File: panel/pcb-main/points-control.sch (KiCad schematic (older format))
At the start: 76 parts

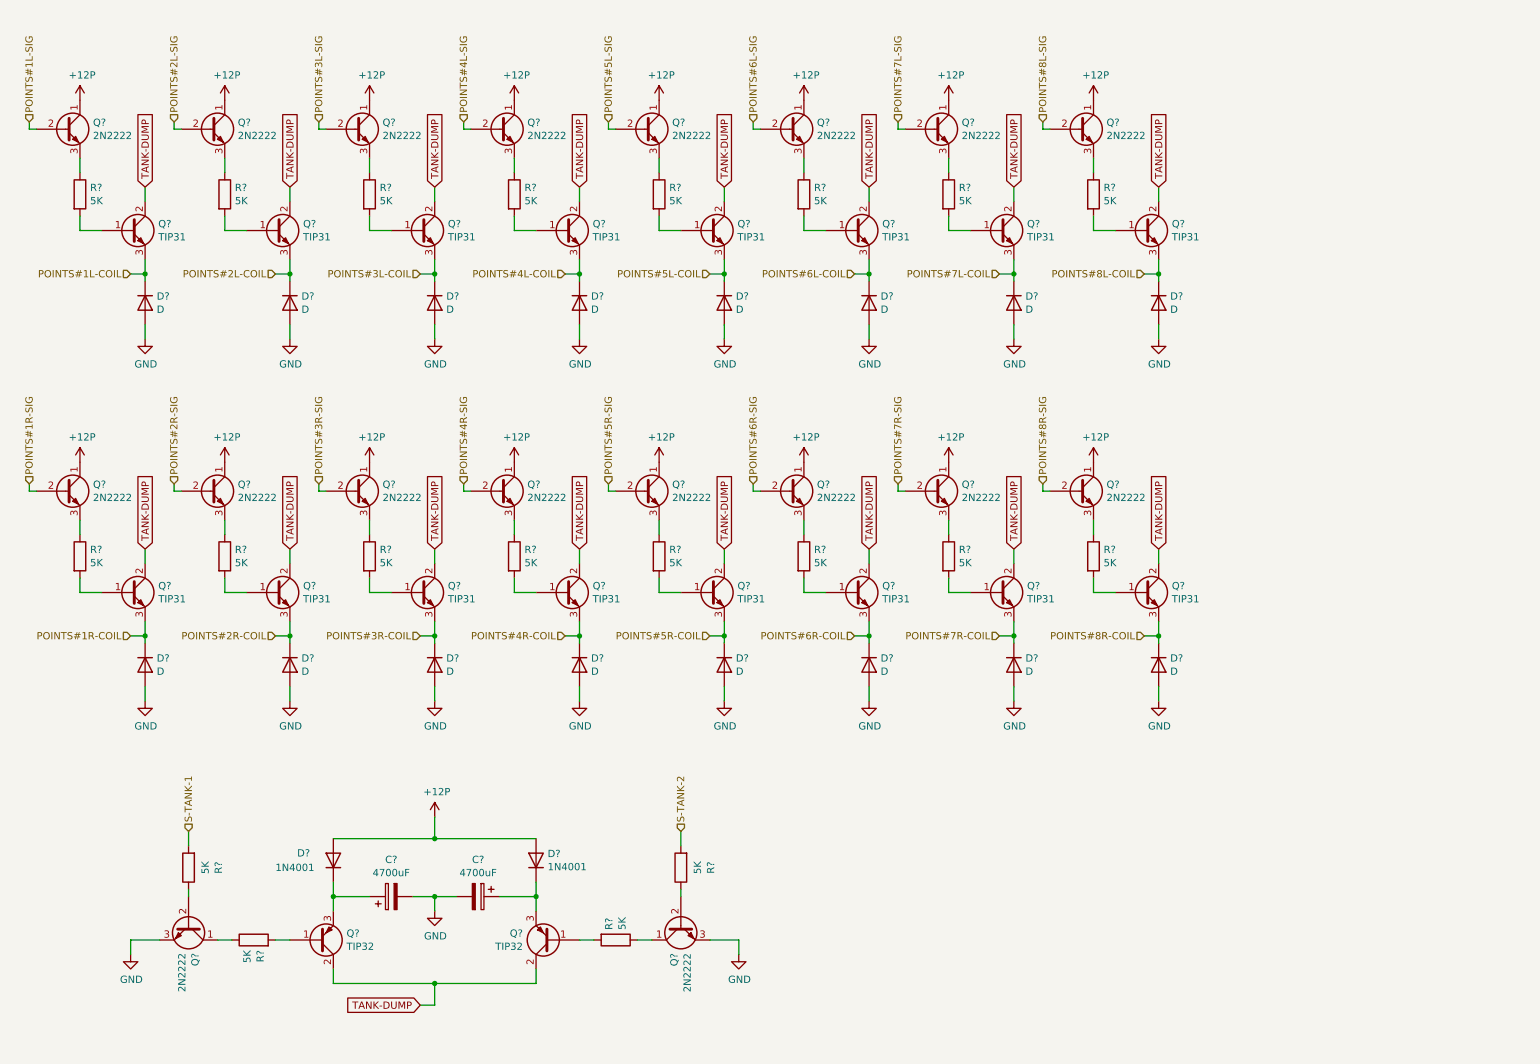
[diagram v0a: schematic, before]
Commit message: PCB Updates and added panel-fw project.
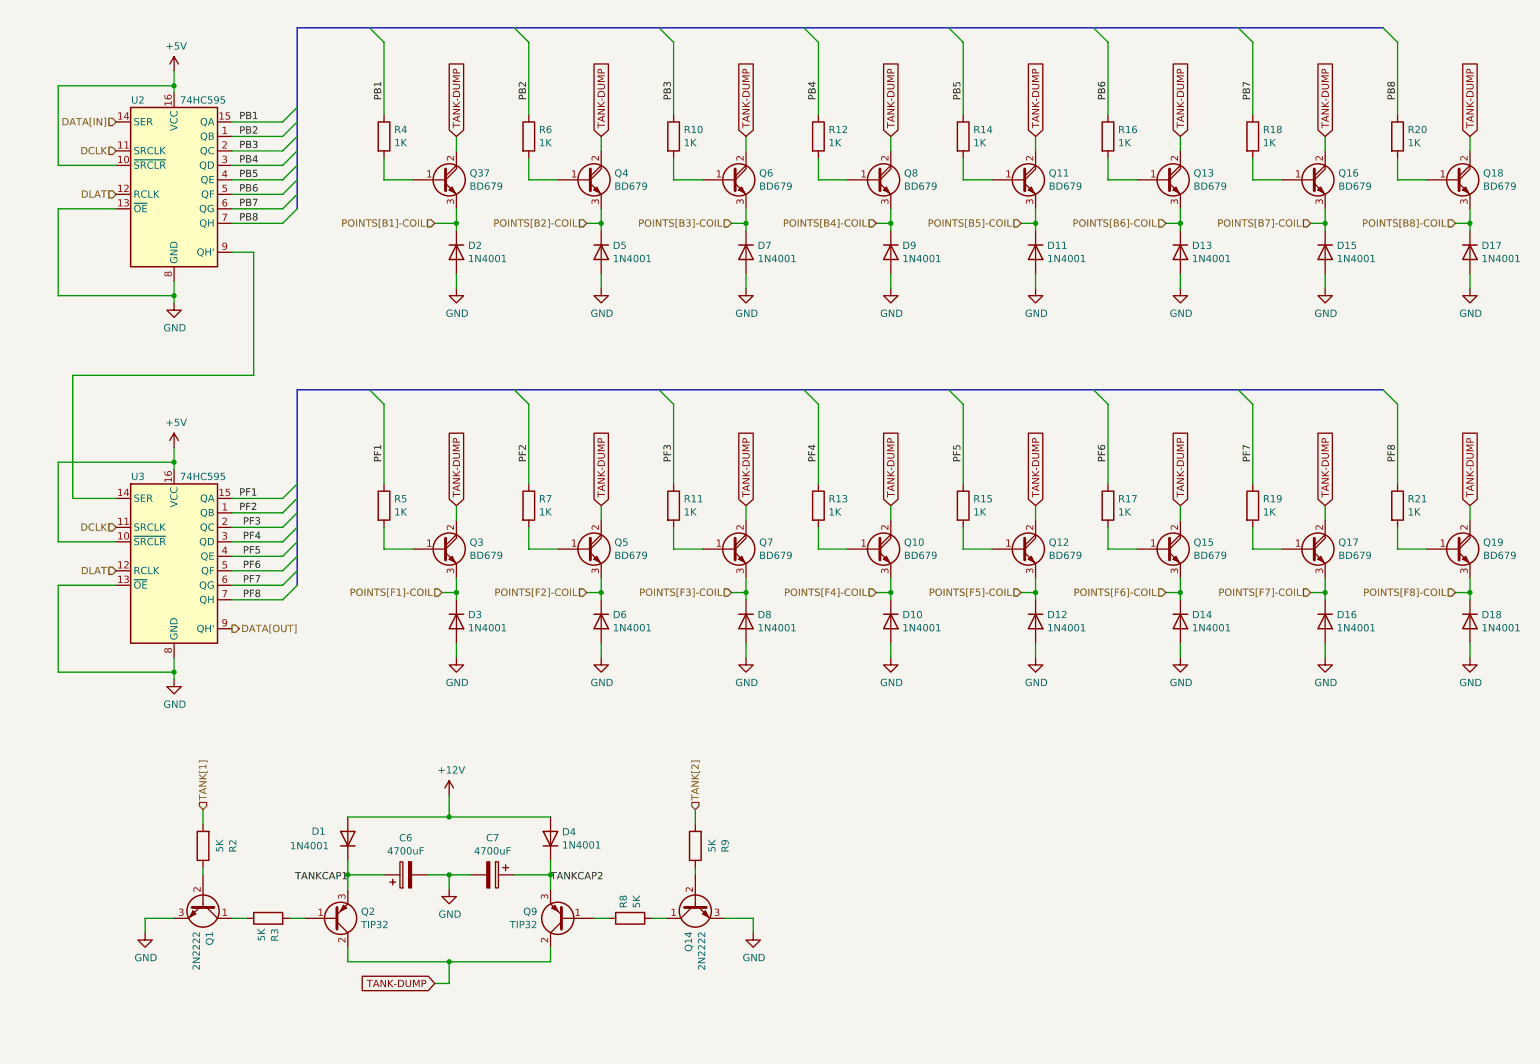
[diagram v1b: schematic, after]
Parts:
- removed Q? (x16): TIP31, Package_TO_SOT_THT:TO-220-3_Vertical, symbol Transistor_BJT:TIP41
- removed Q? (x16): 2N2222, Package_TO_SOT_THT:TO-92_Inline, symbol Transistor_BJT:BC237
- removed R? (x15): 5K, symbol Device:R
- added Q10, Q11, Q12, Q13, Q15, Q16, Q17, Q18, Q19, Q3, Q37, Q4, Q5, Q6, Q7, Q8: BD679, TO_SOT_Packages_THT:TO-126_Vertical, symbol Device:Q_NPN_Darlington_BCE
- added R10, R11, R12, R13, R14, R15, R16, R17, R18, R19, R20, R21, R5, R6, R7: 1K, Resistors_THT:R_Axial_DIN0207_L6.3mm_D2.5mm_P10.16mm_Horizontal, symbol Device:R
- added U2, U3: 74HC595, Housings_DIP:DIP-16_W7.62mm_LongPads, symbol 74xx:74HC595
- C6, C7: renamed from C?; footprint (none) -> Capacitors_THT:CP_Radial_D18.0mm_P7.50mm
- D1, D4: renamed from D?; footprint (none) -> Diodes_THT:D_DO-15_P12.70mm_Horizontal
- D10, D11, D12, D13, D14, D15, D16, D17, D18, D2, D3, D5, D6, D7, D8, D9: renamed from D?; value D -> 1N4001; footprint (none) -> Diodes_THT:D_DO-15_P12.70mm_Horizontal
- Q1, Q14: renamed from Q?; footprint Package_TO_SOT_THT:TO-92_Inline -> TO_SOT_Packages_THT:TO-92_Inline_Wide
- Q2, Q9: renamed from Q?; footprint Package_TO_SOT_THT:TO-220-3_Vertical -> TO_SOT_Packages_THT:TO-220-3_Vertical
- R2, R3, R8, R9: renamed from R?; footprint (none) -> Resistors_THT:R_Axial_DIN0207_L6.3mm_D2.5mm_P10.16mm_Horizontal
- R4: renamed from R?; value 5K -> 1K; footprint (none) -> Resistors_THT:R_Axial_DIN0207_L6.3mm_D2.5mm_P10.16mm_Horizontal
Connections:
- net GND: now also U2.13 (~OE), U2.8 (GND), U3.13 (~OE), U3.8 (GND)
- net TANK-DUMP: now also Q10.2 (C), Q11.2 (C), Q12.2 (C), Q13.2 (C), Q15.2 (C), Q16.2 (C), Q17.2 (C), Q18.2 (C), Q19.2 (C), Q3.2 (C), Q37.2 (C), Q4.2 (C), Q5.2 (C), Q6.2 (C), Q7.2 (C), Q8.2 (C)
- net at R4.2: now also Q37.1 (B)
- net TANKCAP1: now reaches C6.1, D1.1 (K), Q2.3 (E)
- net TANKCAP2: now reaches C7.1, D4.1 (K), Q9.3 (E)
- net PB1: now reaches R4.1
- net PB1: now also U2.15 (QA)
- net +12P renamed +12V
- net POINTS#1L-COIL renamed POINTS[B1]-COIL
- net POINTS[B1]-COIL: now also Q37.3 (E)
- net POINTS#1R-COIL renamed POINTS[F1]-COIL
- net POINTS[F1]-COIL: now also Q3.3 (E)
- net POINTS#2L-COIL renamed POINTS[B2]-COIL
- net POINTS[B2]-COIL: now also Q4.3 (E)
- net POINTS#2R-COIL renamed POINTS[F2]-COIL
- net POINTS[F2]-COIL: now also Q5.3 (E)
- net POINTS#3L-COIL renamed POINTS[B3]-COIL
- net POINTS[B3]-COIL: now also Q6.3 (E)
- net POINTS#3R-COIL renamed POINTS[F3]-COIL
- net POINTS[F3]-COIL: now also Q7.3 (E)
- net POINTS#4L-COIL renamed POINTS[B4]-COIL
- net POINTS[B4]-COIL: now also Q8.3 (E)
- net POINTS#4R-COIL renamed POINTS[F4]-COIL
- net POINTS[F4]-COIL: now also Q10.3 (E)
- net POINTS#5L-COIL renamed POINTS[B5]-COIL
- net POINTS[B5]-COIL: now also Q11.3 (E)
- net POINTS#5R-COIL renamed POINTS[F5]-COIL
- net POINTS[F5]-COIL: now also Q12.3 (E)
- net POINTS#6L-COIL renamed POINTS[B6]-COIL
- net POINTS[B6]-COIL: now also Q13.3 (E)
- net POINTS#6R-COIL renamed POINTS[F6]-COIL
- net POINTS[F6]-COIL: now also Q15.3 (E)
- net POINTS#7L-COIL renamed POINTS[B7]-COIL
- net POINTS[B7]-COIL: now also Q16.3 (E)
- net POINTS#7R-COIL renamed POINTS[F7]-COIL
- net POINTS[F7]-COIL: now also Q17.3 (E)
- net POINTS#8L-COIL renamed POINTS[B8]-COIL
- net POINTS[B8]-COIL: now also Q18.3 (E)
- net POINTS#8R-COIL renamed POINTS[F8]-COIL
- net POINTS[F8]-COIL: now also Q19.3 (E)
- net S-TANK-1 renamed TANK[1]
- net S-TANK-2 renamed TANK[2]
- new net: U2.9 (QH'), U3.14 (SER)
- new net: Q4.1 (B), R6.2
- new net: Q6.1 (B), R10.2
- new net: Q8.1 (B), R12.2
- new net: Q11.1 (B), R14.2
- new net: Q13.1 (B), R16.2
- new net: Q16.1 (B), R18.2
- new net: Q18.1 (B), R20.2
- new net: Q3.1 (B), R5.2
- new net: Q5.1 (B), R7.2
- new net: Q7.1 (B), R11.2
- new net: Q10.1 (B), R13.2
- new net: Q12.1 (B), R15.2
- new net: Q15.1 (B), R17.2
- new net: Q17.1 (B), R19.2
- new net: Q19.1 (B), R21.2
- new net +5V: U2.10 (~SRCLR), U2.16 (VCC), U3.10 (~SRCLR), U3.16 (VCC)
- new net DATA[IN]: U2.14 (SER)
- new net DATA[OUT]: U3.9 (QH')
- new net DCLK: U2.11 (SRCLK), U3.11 (SRCLK)
- new net DLAT: U2.12 (RCLK), U3.12 (RCLK)
- new net PB2: R6.1, U2.1 (QB)
- new net PB3: R10.1, U2.2 (QC)
- new net PB4: R12.1, U2.3 (QD)
- new net PB5: R14.1, U2.4 (QE)
- new net PB6: R16.1, U2.5 (QF)
- new net PB7: R18.1, U2.6 (QG)
- new net PB8: R20.1, U2.7 (QH)
- new net PF1: R5.1, U3.15 (QA)
- new net PF2: R7.1, U3.1 (QB)
- new net PF3: R11.1, U3.2 (QC)
- new net PF4: R13.1, U3.3 (QD)
- new net PF5: R15.1, U3.4 (QE)
- new net PF6: R17.1, U3.5 (QF)
- new net PF7: R19.1, U3.6 (QG)
- new net PF8: R21.1, U3.7 (QH)
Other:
- moved on the sheet: C6, C7, D1, D10, D11, D12, D13, D14, D15, D16, D17, D18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

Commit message: Main PCB Update - MOSFETS on Points, 3 tanks.
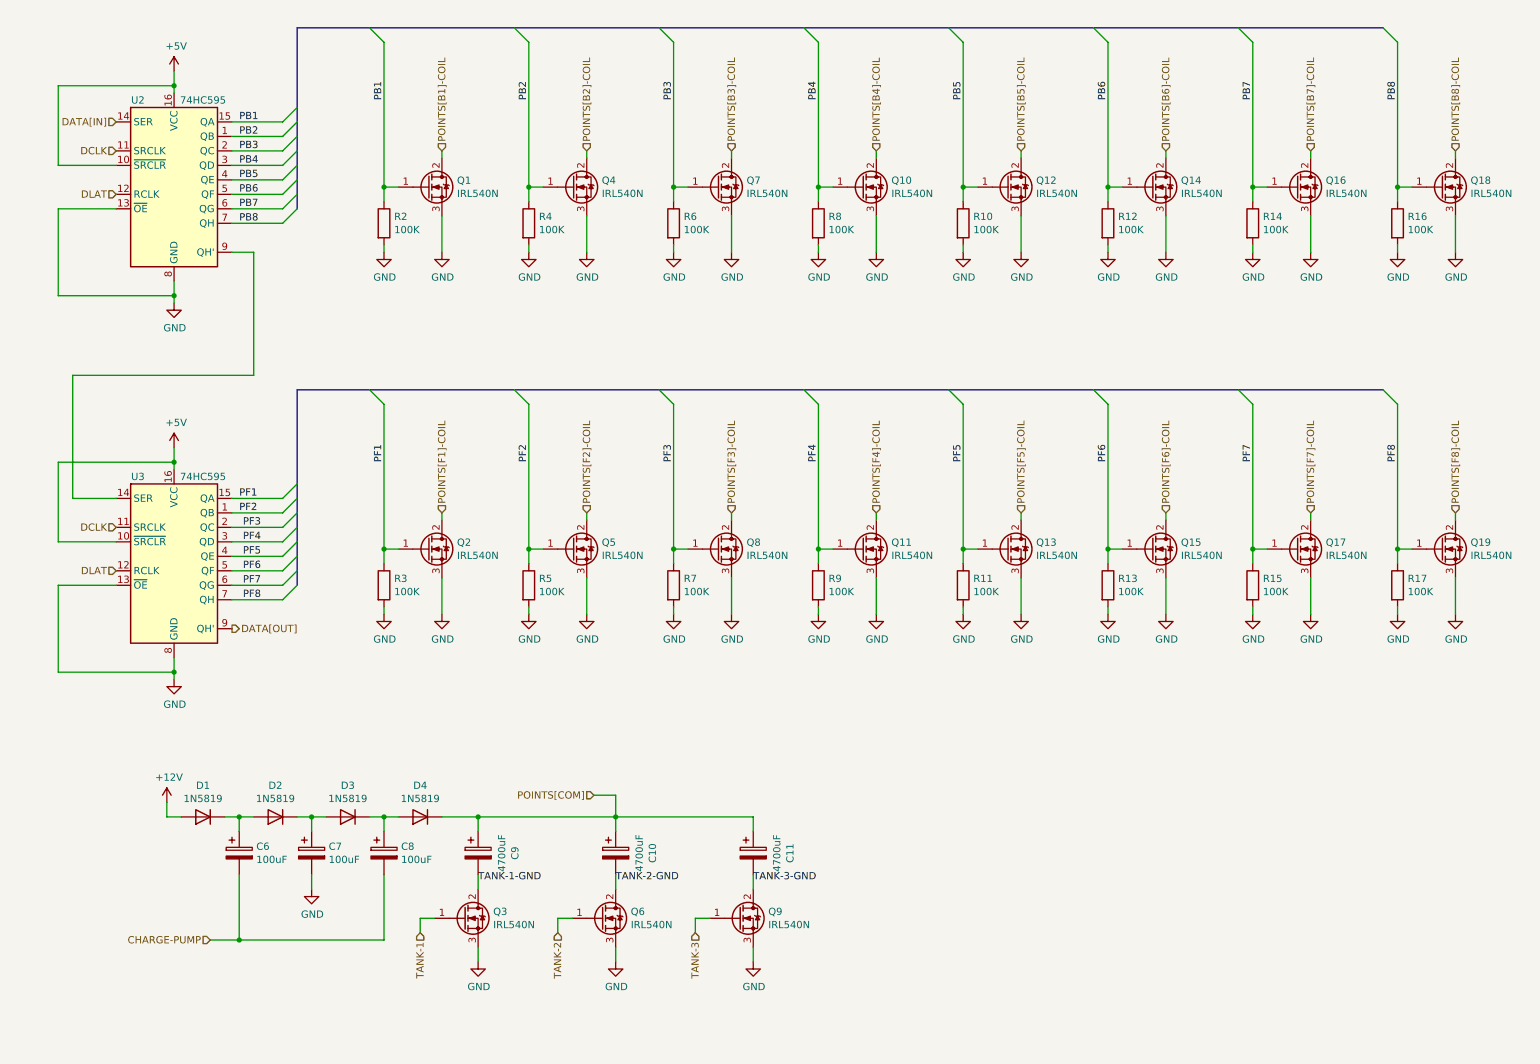
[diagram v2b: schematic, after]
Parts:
- removed D10, D11, D12, D13, D14, D15, D16, D17, D18, D5, D6, D7, D8, D9: 1N4001, Diodes_THT:D_DO-15_P12.70mm_Horizontal, symbol Device:D
- removed Q1, Q14: 2N2222, TO_SOT_Packages_THT:TO-92_Inline_Wide, symbol Transistor_BJT:BC237
- removed Q10, Q11, Q12, Q13, Q15, Q16, Q17, Q18, Q19, Q3, Q37, Q4, Q5, Q6, Q7, Q8: BD679, TO_SOT_Packages_THT:TO-126_Vertical, symbol Device:Q_NPN_Darlington_BCE
- removed Q2, Q9: TIP32, TO_SOT_Packages_THT:TO-220-3_Vertical, symbol Transistor_BJT:TIP42
- removed R18, R19, R20, R21: 1K, Resistors_THT:R_Axial_DIN0207_L6.3mm_D2.5mm_P10.16mm_Horizontal, symbol Device:R
- added C10, C11, C9: 4700uF, Capacitors_THT:CP_Radial_D18.0mm_P7.50mm, symbol Device:CP
- added C8: 100uF, Capacitors_THT:CP_Radial_D8.0mm_P2.50mm, symbol Device:CP
- added Q1, Q10, Q11, Q12, Q13, Q14, Q15, Q16, Q17, Q18, Q19, Q2, Q3, Q4, Q5, Q6, Q7, Q8, Q9: IRL540N, TO_SOT_Packages_THT:TO-220-3_Horizontal, symbol Transistor_FET:IRF540N
- C6, C7: value 4700uF -> 100uF; footprint Capacitors_THT:CP_Radial_D18.0mm_P7.50mm -> Capacitors_THT:CP_Radial_D8.0mm_P2.50mm
- D1, D2, D3, D4: value 1N4001 -> 1N5819
- R10, R11, R12, R13, R14, R15, R16, R17, R4, R5, R6, R7: value 1K -> 100K
- R2, R3, R8, R9: value 5K -> 100K
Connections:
- net TANK[1] is gone; now on net GND: R2.2
- net TANK[2] is gone; now on net GND: R9.2
- net +12V: no longer D4.2 (A)
- net GND: now also R10.2, R11.2, R12.2, R13.2, R14.2, R15.2, R16.2, R17.2, R3.2, R4.2, R5.2, R6.2, R7.2, R8.2, Q1.3 (S), Q10.3 (S), Q11.3 (S), Q12.3 (S), Q13.3 (S), Q14.3 (S), Q15.3 (S), Q16.3 (S), Q17.3 (S), Q18.3 (S), Q19.3 (S), Q2.3 (S), Q3.3 (S), Q4.3 (S), Q5.3 (S), Q6.3 (S), Q7.3 (S), Q8.3 (S), Q9.3 (S); no longer C6.2, D2.2 (A), D3.2 (A)
- net PB1: now also R2.1, Q1.1 (G); no longer R4.1
- net PB2: now also R4.1, Q4.1 (G); no longer R6.1
- net PB3: now also R6.1, Q7.1 (G); no longer R10.1
- net PB4: now also R8.1, Q10.1 (G); no longer R12.1
- net PB5: now also R10.1, Q12.1 (G); no longer R14.1
- net PB6: now also R12.1, Q14.1 (G); no longer R16.1
- net PB7: now also R14.1, Q16.1 (G)
- net PB8: now also R16.1, Q18.1 (G)
- net PF1: now also R3.1, Q2.1 (G); no longer R5.1
- net PF2: now also R5.1, Q5.1 (G); no longer R7.1
- net PF3: now also R7.1, Q8.1 (G); no longer R11.1
- net PF4: now also R9.1, Q11.1 (G); no longer R13.1
- net PF5: now also R11.1, Q13.1 (G); no longer R15.1
- net PF6: now also R13.1, Q15.1 (G); no longer R17.1
- net PF7: now also R15.1, Q17.1 (G)
- net PF8: now also R17.1, Q19.1 (G)
- net POINTS[B1]-COIL: now also Q1.2 (D); no longer D2.1 (K)
- net POINTS[B2]-COIL: now also Q4.2 (D)
- net POINTS[B3]-COIL: now also Q7.2 (D)
- net POINTS[B4]-COIL: now also Q10.2 (D)
- net POINTS[B5]-COIL: now also Q12.2 (D)
- net POINTS[B6]-COIL: now also Q14.2 (D)
- net POINTS[B7]-COIL: now also Q16.2 (D)
- net POINTS[B8]-COIL: now also Q18.2 (D)
- net POINTS[F1]-COIL: now also Q2.2 (D); no longer D3.1 (K)
- net POINTS[F2]-COIL: now also Q5.2 (D)
- net POINTS[F3]-COIL: now also Q8.2 (D)
- net POINTS[F4]-COIL: now also Q11.2 (D)
- net POINTS[F5]-COIL: now also Q13.2 (D)
- net POINTS[F6]-COIL: now also Q15.2 (D)
- net POINTS[F7]-COIL: now also Q17.2 (D)
- net POINTS[F8]-COIL: now also Q19.2 (D)
- net TANKCAP1: no longer names the net of C6.1, D1.1 (K)
- net TANKCAP1: now also D2.2 (A)
- net TANKCAP2: no longer names the net of C7.1
- net TANKCAP2: now also D2.1 (K), D3.2 (A); no longer D4.1 (K)
- new net: C8.1, D3.1 (K), D4.2 (A)
- new net CHARGE-PUMP: C6.2, C8.2
- new net POINTS[COM]: C10.1, C11.1, C9.1, D4.1 (K)
- new net TANK-1: Q3.1 (G)
- new net TANK-1-GND: C9.2, Q3.2 (D)
- new net TANK-2: Q6.1 (G)
- new net TANK-2-GND: C10.2, Q6.2 (D)
- new net TANK-3: Q9.1 (G)
- new net TANK-3-GND: C11.2, Q9.2 (D)

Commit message: Completed all PCBs and added gerber files
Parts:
- removed C10, C11: 4700uF, Capacitors_THT:CP_Radial_D18.0mm_P7.50mm, symbol Device:CP
- removed Q3: IRL540N, TO_SOT_Packages_THT:TO-220-3_Horizontal, symbol Transistor_FET:IRF540N
- added Q3: 2N2219, TO_SOT_Packages_THT:TO-92_Inline_Wide, symbol Transistor_BJT:2N2219
- added R20: 2.2K, Resistors_THT:R_Axial_DIN0207_L6.3mm_D2.5mm_P10.16mm_Horizontal, symbol Device:R
- added R21, R22, R24, R25, R26, R27, R28, R29, R30, R31, R32, R33, R34, R35, R36, R37, R41: 4.7K, Resistors_THT:R_Axial_DIN0207_L6.3mm_D2.5mm_P10.16mm_Horizontal, symbol Device:R
- added R23: 100K, Resistors_THT:R_Axial_DIN0207_L6.3mm_D2.5mm_P10.16mm_Horizontal, symbol Device:R
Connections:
- net TANK-1-GND is gone; now on net GND: C9.2
- net TANK-2-GND is gone; now on net +12V: Q6.2 (D)
- net +12V: now also R23.1
- net CHARGE-PUMP: now also R20.2, R41.2; no longer C6.2, C8.2
- net GND: now also Q3.1 (E); no longer Q6.3 (S)
- net PB1: now also R21.1; no longer Q1.1 (G), R2.1
- net PB2: now also R24.1; no longer Q4.1 (G), R4.1
- net PB3: now also R26.1; no longer Q7.1 (G), R6.1
- net PB4: now also R28.1; no longer Q10.1 (G), R8.1
- net PB5: now also R30.1; no longer Q12.1 (G), R10.1
- net PB6: now also R32.1; no longer Q14.1 (G), R12.1
- net PB7: now also R34.1; no longer Q16.1 (G), R14.1
- net PB8: now also R36.1; no longer Q18.1 (G), R16.1
- net PF1: now also R22.1; no longer Q2.1 (G), R3.1
- net PF2: now also R25.1; no longer Q5.1 (G), R5.1
- net PF3: now also R27.1; no longer Q8.1 (G), R7.1
- net PF4: now also R29.1; no longer Q11.1 (G), R9.1
- net PF5: now also R31.1; no longer Q13.1 (G), R11.1
- net PF6: now also R33.1; no longer Q15.1 (G), R13.1
- net PF7: now also R35.1; no longer Q17.1 (G), R15.1
- net PF8: now also R37.1; no longer Q19.1 (G), R17.1
- net TANK-2: no longer names the net of Q6.1 (G)
- net TANK-2: now also Q3.3 (C), R23.2
- net TANK-3: no longer names the net of Q9.1 (G)
- net TANK-3: now also R41.1
- net TANK-3-GND: no longer names the net of Q9.2 (D)
- net TANK-3-GND: now also C6.2, C8.2, Q6.3 (S)
- new net: Q3.2 (B), R20.1
- new net: Q2.1 (G), R22.2, R3.1
- new net: Q5.1 (G), R25.2, R5.1
- new net: Q1.1 (G), R2.1, R21.2
- new net: Q4.1 (G), R24.2, R4.1
- new net: Q7.1 (G), R26.2, R6.1
- new net: Q10.1 (G), R28.2, R8.1
- new net: Q12.1 (G), R10.1, R30.2
- new net: Q14.1 (G), R12.1, R32.2
- new net: Q16.1 (G), R14.1, R34.2
- new net: Q18.1 (G), R16.1, R36.2
- new net: Q8.1 (G), R27.2, R7.1
- new net: Q11.1 (G), R29.2, R9.1
- new net: Q13.1 (G), R11.1, R31.2
- new net: Q15.1 (G), R13.1, R33.2
- new net: Q17.1 (G), R15.1, R35.2
- new net: Q19.1 (G), R17.1, R37.2
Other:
- moved on the sheet: C6, C7, C8, C9, D1, D2, D3, D4
